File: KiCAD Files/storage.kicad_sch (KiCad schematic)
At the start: 2 parts, among them U1 K230_Rewired, U2 ZDSD04GLGEAG

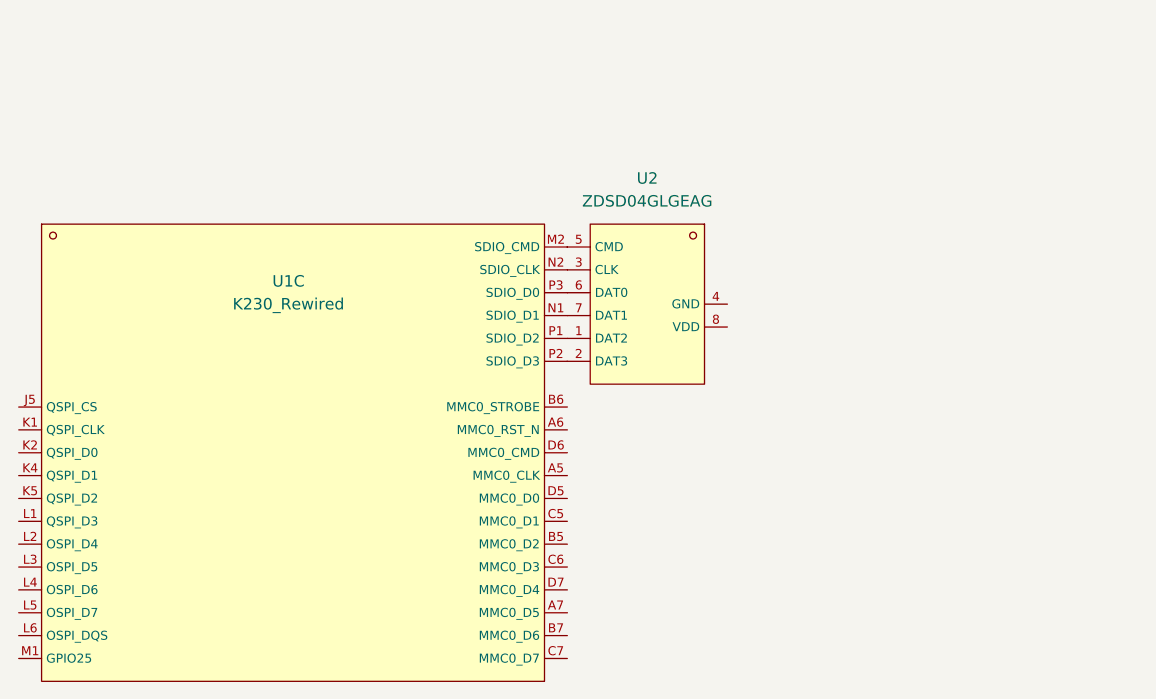
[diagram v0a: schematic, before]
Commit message: added ram and flash
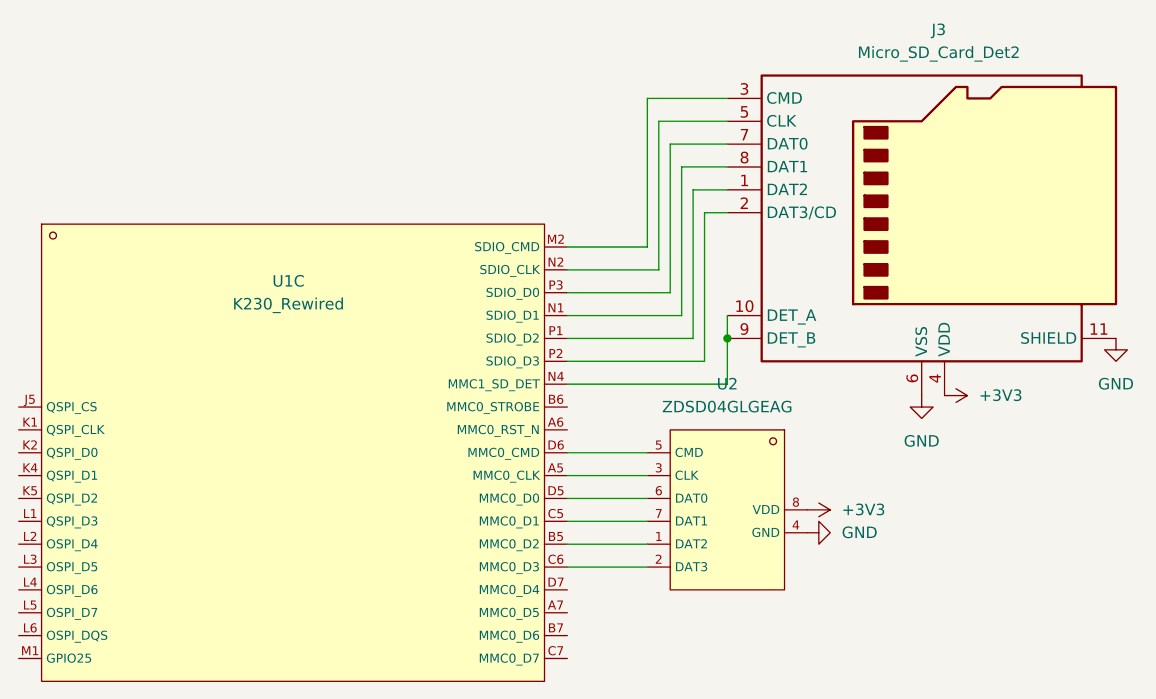
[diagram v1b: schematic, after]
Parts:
- added J3: Micro_SD_Card_Det2, Connector_Card:microSD_HC_Molex_104031-0811, symbol Connector:Micro_SD_Card_Det2
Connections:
- net at U2.1 (DAT2): now also U1.B5 (MMC0_D2); no longer U1.P1 (SDIO_D2)
- net at U2.2 (DAT3): now also U1.C6 (MMC0_D3); no longer U1.P2 (SDIO_D3)
- net at U2.3 (CLK): now also U1.A5 (MMC0_CLK); no longer U1.N2 (SDIO_CLK)
- net GND: now reaches U2.4 (GND)
- net GND: now also J3.11 (SHIELD), J3.6 (VSS)
- net at U2.5 (CMD): now also U1.D6 (MMC0_CMD); no longer U1.M2 (SDIO_CMD)
- net at U2.6 (DAT0): now also U1.D5 (MMC0_D0); no longer U1.P3 (SDIO_D0)
- net at U2.7 (DAT1): now also U1.C5 (MMC0_D1); no longer U1.N1 (SDIO_D1)
- net +3V3: now reaches U2.8 (VDD)
- net +3V3: now also J3.4 (VDD)
- new net: J3.3 (CMD), U1.M2 (SDIO_CMD)
- new net: J3.8 (DAT1), U1.N1 (SDIO_D1)
- new net: J3.5 (CLK), U1.N2 (SDIO_CLK)
- new net: J3.10 (DET_A), J3.9 (DET_B), U1.N4 (MMC1_SD_DET)
- new net: J3.1 (DAT2), U1.P1 (SDIO_D2)
- new net: J3.2 (DAT3/CD), U1.P2 (SDIO_D3)
- new net: J3.7 (DAT0), U1.P3 (SDIO_D0)
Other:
- moved on the sheet: U2
